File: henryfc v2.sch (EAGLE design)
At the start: 20 parts

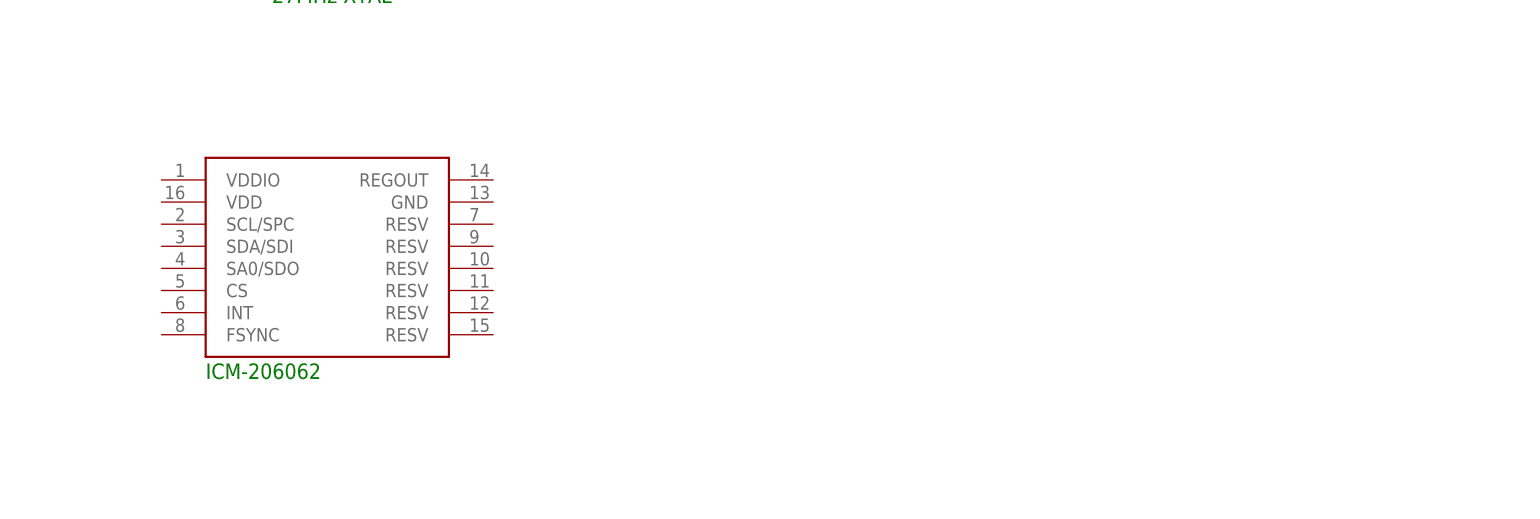
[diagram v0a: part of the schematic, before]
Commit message: updated power, gyro for cleanliness & readability
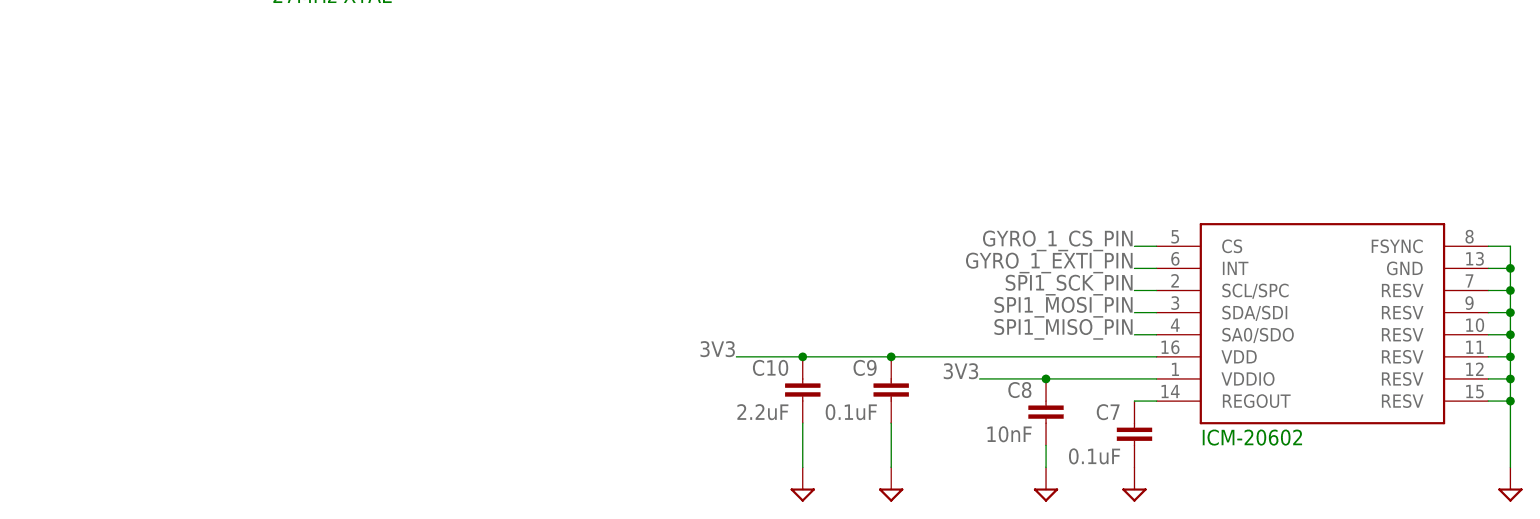
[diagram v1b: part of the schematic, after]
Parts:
- added C10: 2.2uF, rcl:C-EUC0402
- added C7, C9: 0.1uF, rcl:C-EUC0402
- added C8: 10nF, rcl:C-EUC0402
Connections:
- new net GYRO_1_CS_PIN: U$8.CS
- new net GYRO_1_EXTI_PIN: U$8.INT
- new net N$10: C7.1, U$8.REGOUT
- new net SPI1_MISO_PIN: U$8.SA0/SDO
- new net SPI1_MOSI_PIN: U$8.SDA/SDI
- new net SPI1_SCK_PIN: U$8.SCL/SPC
- net 3V3: now also C10.1, C8.1, C9.1, U$8.VDD, U$8.VDDIO
- net GND: now also C10.2, C7.2, C8.2, C9.2, U$8.FSYNC, U$8.GND, U$8.RESV, U$8.RESV@1, U$8.RESV@2, U$8.RESV@3, U$8.RESV@4, U$8.RESV@5
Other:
- note added: "ICM-20602"
- note removed: "ICM-206062"
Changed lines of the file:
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@@
 <part name="U$5" library="HenryFC" deviceset="STM32F722" device=""/>
 <part name="U$7" library="HenryFC" deviceset="MAX7456" device=""/>
-<part name="U$8" library="HenryFC" deviceset="ICM-20602" device=""/>
 <part name="U$9" library="HenryFC" deviceset="ECX-32-8MHZ" device=""/>
 <part name="U$10" library="HenryFC" deviceset="NX3225GA-27MHZ" device=""/>
@@
 <part name="SUPPLY4" library="supply2" library_urn="urn:adsk.eagle:library:372" deviceset="GND" device=""/>
 <part name="SUPPLY5" library="supply2" library_urn="urn:adsk.eagle:library:372" deviceset="GND" device=""/>
+<part name="U$8" library="HenryFC" deviceset="ICM-20602" device=""/>
+<part name="SUPPLY6" library="supply2" library_urn="urn:adsk.eagle:library:372" deviceset="GND" device=""/>
+<part name="C7" library="rcl" library_urn="urn:adsk.eagle:library:334" deviceset="C-EU" device="C0402" package3d_urn="urn:adsk.eagle:package:23626/2" value="0.1uF"/>
+<part name="SUPPLY7" library="supply2" library_urn="urn:adsk.eagle:library:372" deviceset="GND" device=""/>
+<part name="C8" library="rcl" library_urn="urn:adsk.eagle:library:334" deviceset="C-EU" device="C0402" package3d_urn="urn:adsk.eagle:package:23626/2" value="10nF"/>
+<part name="SUPPLY8" library="supply2" library_urn="urn:adsk.eagle:library:372" deviceset="GND" device=""/>
+<part name="C9" library="rcl" library_urn="urn:adsk.eagle:library:334" deviceset="C-EU" device="C0402" package3d_urn="urn:adsk.eagle:package:23626/2" value="0.1uF"/>
+<part name="C10" library="rcl" library_urn="urn:adsk.eagle:library:334" deviceset="C-EU" device="C0402" package3d_urn="urn:adsk.eagle:package:23626/2" value="2.2uF"/>
+<part name="SUPPLY9" library="supply2" library_urn="urn:adsk.eagle:library:372" deviceset="GND" device=""/>
+<part name="SUPPLY10" library="supply2" library_urn="urn:adsk.eagle:library:372" deviceset="GND" device=""/>
 </parts>
 <sheets>
@@
 <text x="-33.02" y="33.02" size="1.778" layer="91">STM32F722RET6</text>
 <text x="167.64" y="55.88" size="1.778" layer="91">MAX7456E</text>
-<text x="167.64" y="2.54" size="1.778" layer="91">ICM-206062</text>
+<text x="281.94" y="-5.08" size="1.778" layer="91">ICM-20602</text>
 </plain>
 <instances>
@@
 <instance part="U$5" gate="G$1" x="-15.24" y="78.74" smashed="yes"/>
 <instance part="U$7" gate="G$1" x="180.34" y="78.74" smashed="yes"/>
-<instance part="U$8" gate="G$1" x="180.34" y="15.24" smashed="yes"/>
 <instance part="U$9" gate="G$1" x="-12.7" y="27.94" smashed="yes" rot="R180"/>
 <instance part="U$10" gate="G$1" x="180.34" y="50.8" smashed="yes" rot="R180"/>
@@
 <instance part="SUPPLY4" gate="GND" x="-167.64" y="22.86" smashed="yes"/>
 <instance part="SUPPLY5" gate="GND" x="-129.54" y="22.86" smashed="yes"/>
+<instance part="U$8" gate="G$1" x="294.64" y="7.62" smashed="yes"/>
+<instance part="SUPPLY6" gate="GND" x="317.5" y="-10.16" smashed="yes"/>
+<instance part="C7" gate="G$1" x="274.32" y="-2.54" smashed="yes">
+<attribute name="NAME" x="272.796" y="-2.159" size="1.778" layer="95" rot="MR0"/>
+<attribute name="VALUE" x="272.796" y="-7.239" size="1.778" layer="96" rot="MR0"/>
+</instance>
+<instance part="SUPPLY7" gate="GND" x="274.32" y="-10.16" smashed="yes"/>
+<instance part="C8" gate="G$1" x="264.16" y="0" smashed="yes">
+<attribute name="NAME" x="262.636" y="0.381" size="1.778" layer="95" rot="MR0"/>
+<attribute name="VALUE" x="262.636" y="-4.699" size="1.778" layer="96" rot="MR0"/>
+</instance>
+<instance part="SUPPLY8" gate="GND" x="264.16" y="-10.16" smashed="yes"/>
+<instance part="C9" gate="G$1" x="246.38" y="2.54" smashed="yes">
+<attribute name="NAME" x="244.856" y="2.921" size="1.778" layer="95" rot="MR0"/>
+<attribute name="VALUE" x="244.856" y="-2.159" size="1.778" layer="96" rot="MR0"/>
+</instance>
+<instance part="C10" gate="G$1" x="236.22" y="2.54" smashed="yes">
+<attribute name="NAME" x="234.696" y="2.921" size="1.778" layer="95" rot="MR0"/>
+<attribute name="VALUE" x="234.696" y="-2.159" size="1.778" layer="96" rot="MR0"/>
+</instance>
+<instance part="SUPPLY9" gate="GND" x="246.38" y="-10.16" smashed="yes"/>
+<instance part="SUPPLY10" gate="GND" x="236.22" y="-10.16" smashed="yes"/>
 </instances>
 <busses>
@@
 <junction x="-129.54" y="25.4"/>
 </segment>
+<segment>
+<pinref part="U$8" gate="G$1" pin="RESV@5"/>
+<wire x1="314.96" y1="0" x2="317.5" y2="0" width="0.1524" layer="91"/>
+<wire x1="317.5" y1="0" x2="317.5" y2="2.54" width="0.1524" layer="91"/>
+<pinref part="U$8" gate="G$1" pin="FSYNC"/>
+<wire x1="317.5" y1="2.54" x2="317.5" y2="5.08" width="0.1524" layer="91"/>
+<wire x1="317.5" y1="5.08" x2="317.5" y2="7.62" width="0.1524" layer="91"/>
+<wire x1="317.5" y1="7.62" x2="317.5" y2="10.16" width="0.1524" layer="91"/>
+<wire x1="317.5" y1="10.16" x2="317.5" y2="12.7" width="0.1524" layer="91"/>
+<wire x1="317.5" y1="12.7" x2="317.5" y2="15.24" width="0.1524" layer="91"/>
+<wire x1="317.5" y1="15.24" x2="317.5" y2="17.78" width="0.1524" layer="91"/>
+<wire x1="317.5" y1="17.78" x2="314.96" y2="17.78" width="0.1524" layer="91"/>
+<pinref part="U$8" gate="G$1" pin="GND"/>
+<wire x1="314.96" y1="15.24" x2="317.5" y2="15.24" width="0.1524" layer="91"/>
+<junction x="317.5" y="15.24"/>
+<pinref part="U$8" gate="G$1" pin="RESV"/>
+<wire x1="314.96" y1="12.7" x2="317.5" y2="12.7" width="0.1524" layer="91"/>
+<junction x="317.5" y="12.7"/>
+<pinref part="U$8" gate="G$1" pin="RESV@1"/>
+<wire x1="314.96" y1="10.16" x2="317.5" y2="10.16" width="0.1524" layer="91"/>
+<junction x="317.5" y="10.16"/>
+<pinref part="U$8" gate="G$1" pin="RESV@2"/>
+<wire x1="314.96" y1="7.62" x2="317.5" y2="7.62" width="0.1524" layer="91"/>
+<junction x="317.5" y="7.62"/>
+<pinref part="U$8" gate="G$1" pin="RESV@3"/>
+<wire x1="314.96" y1="5.08" x2="317.5" y2="5.08" width="0.1524" layer="91"/>
+<junction x="317.5" y="5.08"/>
+<pinref part="U$8" gate="G$1" pin="RESV@4"/>
+<wire x1="314.96" y1="2.54" x2="317.5" y2="2.54" width="0.1524" layer="91"/>
+<junction x="317.5" y="2.54"/>
+<pinref part="SUPPLY6" gate="GND" pin="GND"/>
+<wire x1="317.5" y1="0" x2="317.5" y2="-7.62" width="0.1524" layer="91"/>
+<junction x="317.5" y="0"/>
+</segment>
+<segment>
+<pinref part="SUPPLY7" gate="GND" pin="GND"/>
+<pinref part="C7" gate="G$1" pin="2"/>
+</segment>
+<segment>
+<pinref part="SUPPLY8" gate="GND" pin="GND"/>
+<pinref part="C8" gate="G$1" pin="2"/>
+<wire x1="264.16" y1="-7.62" x2="264.16" y2="-5.08" width="0.1524" layer="91"/>
+</segment>
+<segment>
+<pinref part="C9" gate="G$1" pin="2"/>
+<wire x1="246.38" y1="-2.54" x2="246.38" y2="-7.62" width="0.1524" layer="91"/>
+<pinref part="SUPPLY9" gate="GND" pin="GND"/>
+</segment>
+<segment>
+<pinref part="C10" gate="G$1" pin="2"/>
+<wire x1="236.22" y1="-2.54" x2="236.22" y2="-7.62" width="0.1524" layer="91"/>
+<pinref part="SUPPLY10" gate="GND" pin="GND"/>
+</segment>
 </net>
 <net name="N$2" class="0">
@@
 <label x="-116.84" y="33.02" size="1.778" layer="95"/>
 </segment>
-</net>
+<segment>
+<pinref part="U$8" gate="G$1" pin="VDDIO"/>
+<pinref part="C8" gate="G$1" pin="1"/>
+<wire x1="264.16" y1="2.54" x2="276.86" y2="2.54" width="0.1524" layer="91"/>
+<wire x1="264.16" y1="2.54" x2="256.54" y2="2.54" width="0.1524" layer="91"/>
+<junction x="264.16" y="2.54"/>
+<label x="256.54" y="2.54" size="1.778" layer="95" rot="MR0"/>
+</segment>
+<segment>
+<pinref part="U$8" gate="G$1" pin="VDD"/>
+<pinref part="C9" gate="G$1" pin="1"/>
+<wire x1="276.86" y1="5.08" x2="246.38" y2="5.08" width="0.1524" layer="91"/>
+<pinref part="C10" gate="G$1" pin="1"/>
+<wire x1="246.38" y1="5.08" x2="236.22" y2="5.08" width="0.1524" layer="91"/>
+<junction x="246.38" y="5.08"/>
+<wire x1="236.22" y1="5.08" x2="228.6" y2="5.08" width="0.1524" layer="91"/>
+<junction x="236.22" y="5.08"/>
+<label x="228.6" y="5.08" size="1.778" layer="95" rot="MR0"/>
+</segment>
+</net>
+<net name="GYRO_1_CS_PIN" class="0">
+<segment>
+<pinref part="U$8" gate="G$1" pin="CS"/>
+<wire x1="276.86" y1="17.78" x2="274.32" y2="17.78" width="0.1524" layer="91"/>
+<label x="274.32" y="17.78" size="1.778" layer="95" rot="MR0"/>
+</segment>
+</net>
+<net name="GYRO_1_EXTI_PIN" class="0">
+<segment>
+<pinref part="U$8" gate="G$1" pin="INT"/>
+<wire x1="276.86" y1="15.24" x2="274.32" y2="15.24" width="0.1524" layer="91"/>
+<label x="274.32" y="15.24" size="1.778" layer="95" rot="MR0"/>
+</segment>
+</net>
+<net name="SPI1_SCK_PIN" class="0">
+<segment>
+<pinref part="U$8" gate="G$1" pin="SCL/SPC"/>
+<wire x1="276.86" y1="12.7" x2="274.32" y2="12.7" width="0.1524" layer="91"/>
+<label x="274.32" y="12.7" size="1.778" layer="95" rot="MR0"/>
+</segment>
+</net>
+<net name="SPI1_MOSI_PIN" class="0">
+<segment>
+<pinref part="U$8" gate="G$1" pin="SDA/SDI"/>
+<wire x1="276.86" y1="10.16" x2="274.32" y2="10.16" width="0.1524" layer="91"/>
+<label x="274.32" y="10.16" size="1.778" layer="95" rot="MR0"/>
+</segment>
+</net>
+<net name="SPI1_MISO_PIN" class="0">
+<segment>
+<pinref part="U$8" gate="G$1" pin="SA0/SDO"/>
+<wire x1="276.86" y1="7.62" x2="274.32" y2="7.62" width="0.1524" layer="91"/>
+<label x="274.32" y="7.62" size="1.778" layer="95" rot="MR0"/>
+</segment>
+</net>
+<net name="N$10" class="0">
+<segment>
+<pinref part="U$8" gate="G$1" pin="REGOUT"/>
+<wire x1="276.86" y1="0" x2="274.32" y2="0" width="0.1524" layer="91"/>
+<pinref part="C7" gate="G$1" pin="1"/>
+</segment>
+</net>

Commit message: more schematic update
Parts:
- added C11, C12, C13, C16, C17, C18: 0.1uF, rcl:C-EUC0402
- added C14: 2.2uF, rcl:C-EUC0402
- added C15: 1uF, rcl:C-EUC0402
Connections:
- new net N$3: C18.1, U$5.NRST
- new net OSC_IN: U$5.PH0-OSC_IN
- new net OSC_OUT: U$5.PH1-OSC_OUT
- net 3V3: now also C11.1, C12.1, C13.1, C14.1, C15.1, C16.1, C17.1, U$5.VCAP_1, U$5.VDD, U$5.VDD@1, U$5.VDD@2, U$5.VDD@3, U$5.VDDA
- net GND: now also C11.2, C12.2, C13.2, C14.2, C15.2, C16.2, C17.2, C18.2, U$5.VSS, U$5.VSS@1, U$5.VSS@2, U$5.VSS@3, U$5.VSSA

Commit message: FINALIZE SCHEMATIC V2
much clean
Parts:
- added C19, C20, C21, C22: 0.1uF, rcl:C-EUC0402
- added C23, C24: 22uF, rcl:C-EUC0402
- added LED1: KB_DELPS2.12-QHRI-24-Z555-10-S, SamacSys_Parts:KB_DELPS2.12-QHRI-24-Z555-10-S
- added LED2: KR_DELPS1.22-UHVI-26-H3Q4, SamacSys_Parts:KR_DELPS1.22-UHVI-26-H3Q4
- added R10, R11, R9: 1K, rcl:R-US_R0402
- added R5, R8: 10k, rcl:R-US_R0402
- added R6, R7: 75, rcl:R-US_R0402
- added TP1, TP2, TP3, TP4: TESTPOINT, HenryFC:TESTPOINT
- added U$11: BOOT_JUMPER, HenryFC:BOOT_JUMPER
- added U$13, U$14, U$15, U$19, U$20, U$21, U$22, U$23, U$24, U$25, U$26, U$27, U$28, U$29, U$30, U$31, U$32, U$33, U$34, U$35, U$36: SOLDERPAD, HenryFC:SOLDERPAD
- added U$37, U$38, U$39, U$40, U$41, U$42, U$43, U$44, U$45, U$46, U$47, U$48, U$49, U$50, U$51, U$52, U$53, U$54, U$55, U$56, U$57, U$58, U$59: POWER, HenryFC:POWER
- added X1: SM07B-SRSS-TB, con-jst:SM07B-SRSS-TB
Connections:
- new net BOOT: R5.2, U$11. , U$5.BOOT0
- new net CAM_S: C21.1, U$31. , U$7.VIN
- new net CLKIN: U$10.CLKIN, U$7.CLKIN
- new net CURRENT_METER_ADC_PIN: U$5.PC4, X1.7
- new net GYRO1_CS_PIN: U$5.PC2
- new net GYRO1_EXTI_PIN: U$5.PC3
- new net LED1: LED1.A, U$5.PA14
- new net LED_STRIP: U$23. , U$5.PA15
- new net M1: U$5.PC6, X1.3
- new net M2: U$5.PC7, X1.4
- new net M3: U$5.PC8, X1.5
- new net M4: U$5.PC9, X1.6
- new net MAX7456_SPI_CS_PIN: U$5.PB10, U$7.!CS
- new net N$11: C24.2, R7.2
- new net N$14: LED1.K, R10.1
- new net N$15: LED2.K, R9.1
- new net N$17: U$5.PB12
- new net N$22: U$5.PC1
- new net N$7: C23.1, U$7.SAG
- new net N$9: C21.2, R6.2
- new net RX1: U$34. , U$5.PA10
- new net RX2: U$24. , U$5.PA3
- new net RX3: U$28. , U$5.PC11
- new net RX4: U$32. , U$5.PA1
- new net RX5: U$5.PD2
- new net SPI2_MISO_PIN: U$5.PB14, U$7.SDOUT
- new net SPI2_MOSI_PIN: U$5.PB15, U$7.SDIN
- new net SPI2_SCK_PIN: U$5.PB13, U$7.SCLK
- new net TX1: U$36. , U$5.PA9
- new net TX2: U$22. , U$5.PA2
- new net TX3: U$26. , U$5.PC10
- new net TX4: U$30. , U$5.PA0-WKUP
- new net TX5: U$5.PC12
- new net VBAT_ADC_PIN: R11.2, R8.1, U$5.PC0
- new net VTX_S: C24.1, U$29. , U$7.VOUT
- new net XFB: U$10.XFB, U$7.XFB
- net 3V3: now also LED2.A, TP2. , U$11.  , U$37.  , U$41.  , U$53.  , U$54.  , U$56.  , U$59.  
- net 5V: now also C19.1, C20.1, C22.1, TP1. , U$15. , U$38.  , U$42.  , U$50.  , U$57.  , U$58.  , U$7.AVDD, U$7.DVDD, U$7.PVDD
- net 5V_REG-A: now also TP4. , U$44.  , U$46.  , U$51.  
- net 5V_REG-B: now also TP3. , U$13. , U$14. , U$25. , U$43.  , U$47.  
- net 5V_USB: now also U$49.  , U$52.  
- net GND: now also C19.2, C20.2, C22.2, C23.2, R10.2, R11.1, R5.1, R6.1, R7.1, R9.2, U$19. , U$20. , U$21. , U$27. , U$35. , U$7.AGND, U$7.DGND, U$7.PGND, X1.1
- net OSC_IN: now also U$9.OSC_IN
- net OSC_OUT: now also U$9.OSC_OUT
- net OTG_FS_DM: now also U$5.PA11
- net OTG_FS_DP: now also U$5.PA12
- net SPI1_MISO_PIN: now also U$5.PA6
- net SPI1_MOSI_PIN: now also U$5.PA7
- net SPI1_SCK_PIN: now also U$5.PA5
- net VCC: now also R8.2, U$33. , U$39.  , U$40.  , U$45.  , U$48.  , U$55.  , X1.2
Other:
- note added: "27MHz"
- note added: "5V_REG-A POWER FOR GYRO, 3.3V, RX"
- note added: "5V_REG-B POWER FOR PERIPHERALS, CAMERA, VTX, PADS"
- note added: "8MHz"
- note added: "BOOT JUMPER"
- note added: "CIRCLE = TEST PAD"
- note added: "ESC CONNECTOR"
- note added: "GROUND PADS"
- note added: "SQUARE = SOLDER PAD"
- note added: "STATUS LED"
- note added: "UART SOLDER PADS"
- note added: "VCC VOLTAGE DIVIDER"
- note removed: "27MHz XTAL"
- note removed: "8MHz XTAL"
- moved on the sheet: C1, C10, C11, C12, C13, C14, C15, C16, C17, C18, C2, C3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
